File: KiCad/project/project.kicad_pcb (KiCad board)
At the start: 4 copper layers, 40 x 45 mm, 29 parts, among them P1 TB002-500-05BE, U1 DRV8313PWPR

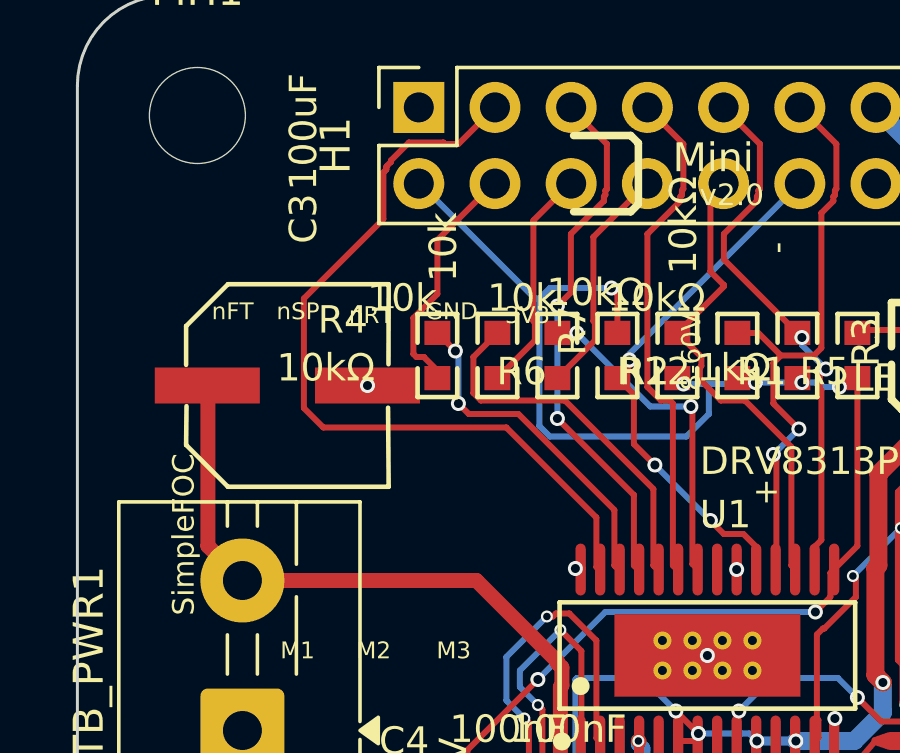
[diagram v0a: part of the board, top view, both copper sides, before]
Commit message: PCB: clear the last C3/R4 overlap (move R4 up, re-route EN1/EN1H)
The bulk cap C3's 9.4mm courtyard / 3.5mm-wide GND pad collided with the
leftmost EN resistor R4 (1 courtyard_overlap + 1 clearance 0.148mm). C3 is
boxed (IN1 routing below-left, board edge left), and the EN row is packed
at 2mm pitch against R12, so neither could shift toward the other.

Moved R4 up 1.6mm (146,100 -> 146,98.4) so its courtyard clears C3's
Y-band entirely, then re-routed its two simple 2-point nets EN1 (U1.26<->R4.2)
and EN1H (H1.4<->R4.1).

Result: 0 error-severity DRC items (was 2), 0 shorts, 0 unconnected, all 92
nets connected, net parity unchanged. The board is now electrically clean;
the 249 remaining DRC items are all cosmetic warnings (silk overlap/over
copper, text height, HTSSOP padstack) -- import artifacts to be cleaned in
a separate silk/text pass.

Co-Authored-By: Claude Opus 4.8 (1M context) <noreply@anthropic.com>
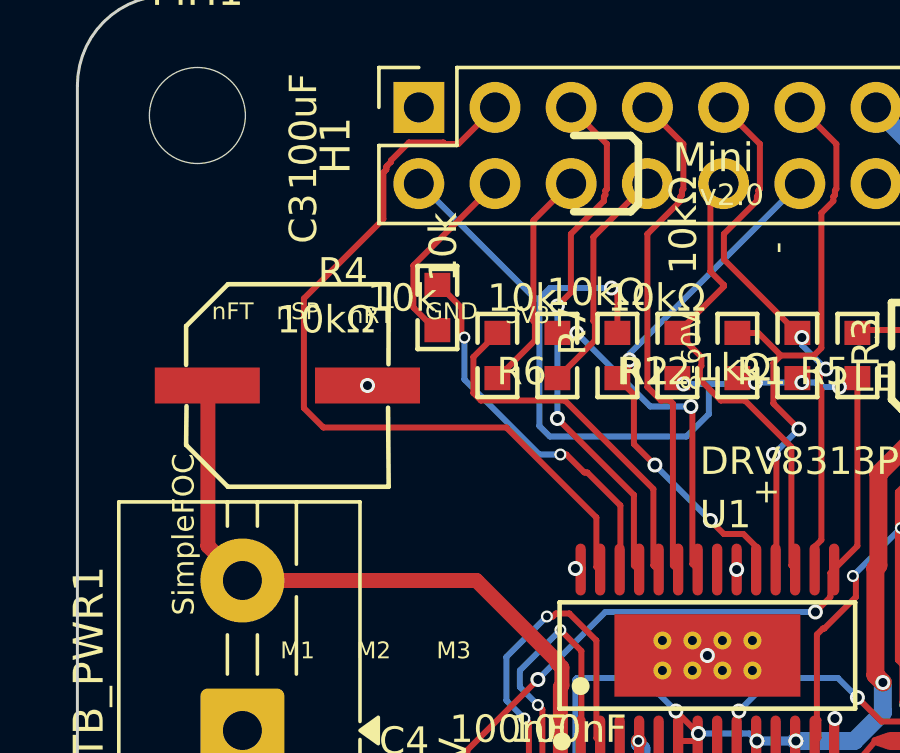
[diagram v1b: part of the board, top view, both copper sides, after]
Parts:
- moved R4 1.60 mm to (146.0, 98.4)
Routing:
- net EN1H: track 8.12 -> 6.43 mm
- net EN1: track 11.4 -> 12.7 mm
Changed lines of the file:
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@@
 	(footprint "R0603"
 		(layer "F.Cu")
-		(at 146 100 90)
+		(at 146 98.4 90)
 		(property "Reference" "R4"
 			(at 1.7221 -3.9853 0)
@@
 			(polygon
 				(pts
-					(xy 136.805 100.45) (xy 137.605 100.45) (xy 137.655 100.4) (xy 137.655 100.172) (xy 137.285 100.172)
-					(xy 137.285 99.842) (xy 137.655 99.842) (xy 137.655 99.6) (xy 137.605 99.55) (xy 136.805 99.55)
-					(xy 136.755 99.6) (xy 136.755 100.4)
+					(xy 136.805 98.85) (xy 137.605 98.85) (xy 137.655 98.8) (xy 137.655 98.572) (xy 137.285 98.572)
+					(xy 137.285 98.242) (xy 137.655 98.242) (xy 137.655 98) (xy 137.605 97.95) (xy 136.805 97.95) (xy 136.755 98)
+					(xy 136.755 98.8)
 				)
 			)
@@
 			(polygon
 				(pts
-					(xy 138.355 100.4) (xy 138.355 100.172) (xy 138.735 100.172) (xy 138.735 99.842) (xy 138.355 99.842)
-					(xy 138.355 99.6) (xy 138.405 99.55) (xy 139.195 99.55) (xy 139.245 99.6) (xy 139.245 100.4) (xy 139.195 100.45)
-					(xy 138.405 100.45)
+					(xy 138.355 98.8) (xy 138.355 98.572) (xy 138.735 98.572) (xy 138.735 98.242) (xy 138.355 98.242)
+					(xy 138.355 98) (xy 138.405 97.95) (xy 139.195 97.95) (xy 139.245 98) (xy 139.245 98.8) (xy 139.195 98.85)
+					(xy 138.405 98.85)
 				)
 			)
@@
 			(polygon
 				(pts
-					(xy 138.8 99.6) (xy 138.8 100.4) (xy 137.2 100.4) (xy 137.2 99.6)
+					(xy 138.8 98) (xy 138.8 98.8) (xy 137.2 98.8) (xy 137.2 98)
 				)
 			)
@@
 			(polygon
 				(pts
-					(xy 137.2 99.6) (xy 137.2 100.4) (xy 137.5 100.4) (xy 137.5 99.6)
+					(xy 137.2 98) (xy 137.2 98.8) (xy 137.5 98.8) (xy 137.5 98)
 				)
 			)
@@
 			(polygon
 				(pts
-					(xy 138.8 99.6) (xy 138.8 100.4) (xy 138.5 100.4) (xy 138.5 99.6)
+					(xy 138.8 98) (xy 138.8 98.8) (xy 138.5 98.8) (xy 138.5 98)
 				)
 			)
@@
 	)
 	(segment
-		(start 152.0749 107.1344)
-		(end 152.05 107.15)
+		(start 146 97.6)
+		(end 146 97.6466)
 		(width 0.2)
 		(layer "F.Cu")
@@
 	)
 	(segment
-		(start 152.05 107.15)
-		(end 151.9 107)
+		(start 146.8 98.4)
+		(end 146 97.6)
 		(width 0.2)
 		(layer "F.Cu")
@@
 	)
 	(segment
-		(start 151.9 105.15)
-		(end 148.7 101.95)
+		(start 146.9 99.4)
+		(end 146.8 99.3)
 		(width 0.2)
 		(layer "F.Cu")
@@
 	)
 	(segment
-		(start 151.9 107)
-		(end 151.9 105.15)
+		(start 146.8 99.3)
+		(end 146.8 98.4)
+		(width 0.2)
+		(layer "F.Cu")
+		(net "EN1")
+	)
+	(segment
+		(start 152.0749 107.1344)
+		(end 152.1 107.1)
 		(width 0.2)
 		(layer "F.Cu")
@@
 	)
 	(segment
-		(start 148.7 101.95)
-		(end 147.05 101.95)
+		(start 151 103.9)
+		(end 150.9 103.9)
 		(width 0.2)
 		(layer "F.Cu")
@@
 	)
 	(segment
-		(start 146.6 99.85)
-		(end 146 99.25)
+		(start 152.1 105)
+		(end 151 103.9)
 		(width 0.2)
 		(layer "F.Cu")
@@
 	)
 	(segment
-		(start 147.05 101.95)
-		(end 146.7 101.6)
+		(start 152.1 107.1)
+		(end 152.1 105)
+		(width 0.2)
+		(layer "F.Cu")
+		(net "EN1")
+	)
+	(segment
+		(start 150.9 103.9)
+		(end 150.3 103.3)
+		(width 0.2)
+		(layer "F.Cu")
+		(net "EN1")
+	)
+	(segment
+		(start 150.3 103.3)
+		(end 150.1 103.3)
 		(width 0.2)
 		(layer "F.Cu")
@@
 	)
 	(via
-		(at 146.7 101.6)
-		(size 0.5)
-		(drill 0.3)
+		(at 150.1 103.3)
+		(size 0.4)
+		(drill 0.25)
 		(layers "F.Cu" "B.Cu")
 		(tenting
@@
 	)
 	(via
-		(at 146.6 99.85)
-		(size 0.5)
-		(drill 0.3)
+		(at 146.9 99.4)
+		(size 0.4)
+		(drill 0.25)
 		(layers "F.Cu" "B.Cu")
 		(tenting
@@
 	)
 	(segment
-		(start 146.7 99.95)
-		(end 146.6 99.85)
+		(start 146.9 100.8)
+		(end 146.9 99.4)
 		(width 0.2)
 		(layer "B.Cu")
@@
 	)
 	(segment
-		(start 146.7 101.6)
-		(end 146.7 99.95)
+		(start 149.4 103.3)
+		(end 146.9 100.8)
+		(width 0.2)
+		(layer "B.Cu")
+		(net "EN1")
+	)
+	(segment
+		(start 150.1 103.3)
+		(end 149.4 103.3)
 		(width 0.2)
 		(layer "B.Cu")
@@
 	)
 	(segment
-		(start 146 97.95)
-		(end 145.2 98.75)
-		(width 0.2)
-		(layer "F.Cu")
-		(net "EN1H")
-	)
-	(segment
-		(start 145.2 98.75)
-		(end 145.2 99.95)
-		(width 0.2)
-		(layer "F.Cu")
-		(net "EN1H")
-	)
-	(segment
 		(start 147.92 94.27)
-		(end 147.9 94.25)
-		(width 0.2)
-		(layer "F.Cu")
-		(net "EN1H")
-	)
-	(segment
-		(start 146 96.15)
-		(end 146 97.95)
-		(width 0.2)
-		(layer "F.Cu")
-		(net "EN1H")
-	)
-	(segment
-		(start 147.9 94.25)
-		(end 146 96.15)
+		(end 147.9 94.3)
 		(width 0.2)
 		(layer "F.Cu")
@@
 	)
 	(segment
-		(start 145.55 100.05)
-		(end 146 100.5)
+		(start 147.9 94.3)
+		(end 145.2 97)
 		(width 0.2)
 		(layer "F.Cu")
@@
 	)
 	(segment
-		(start 145.2 99.95)
-		(end 145.3 100.05)
+		(start 145.2 98.4)
+		(end 146 99.2)
 		(width 0.2)
 		(layer "F.Cu")
@@
 	)
 	(segment
-		(start 145.3 100.05)
-		(end 145.55 100.05)
+		(start 146 99.2)
+		(end 146 99.1534)
 		(width 0.2)
 		(layer "F.Cu")
@@
 	)
 	(segment
-		(start 146 100.5)
-		(end 146 100.75)
+		(start 145.2 97)
+		(end 145.2 98.4)
 		(width 0.2)
 		(layer "F.Cu")

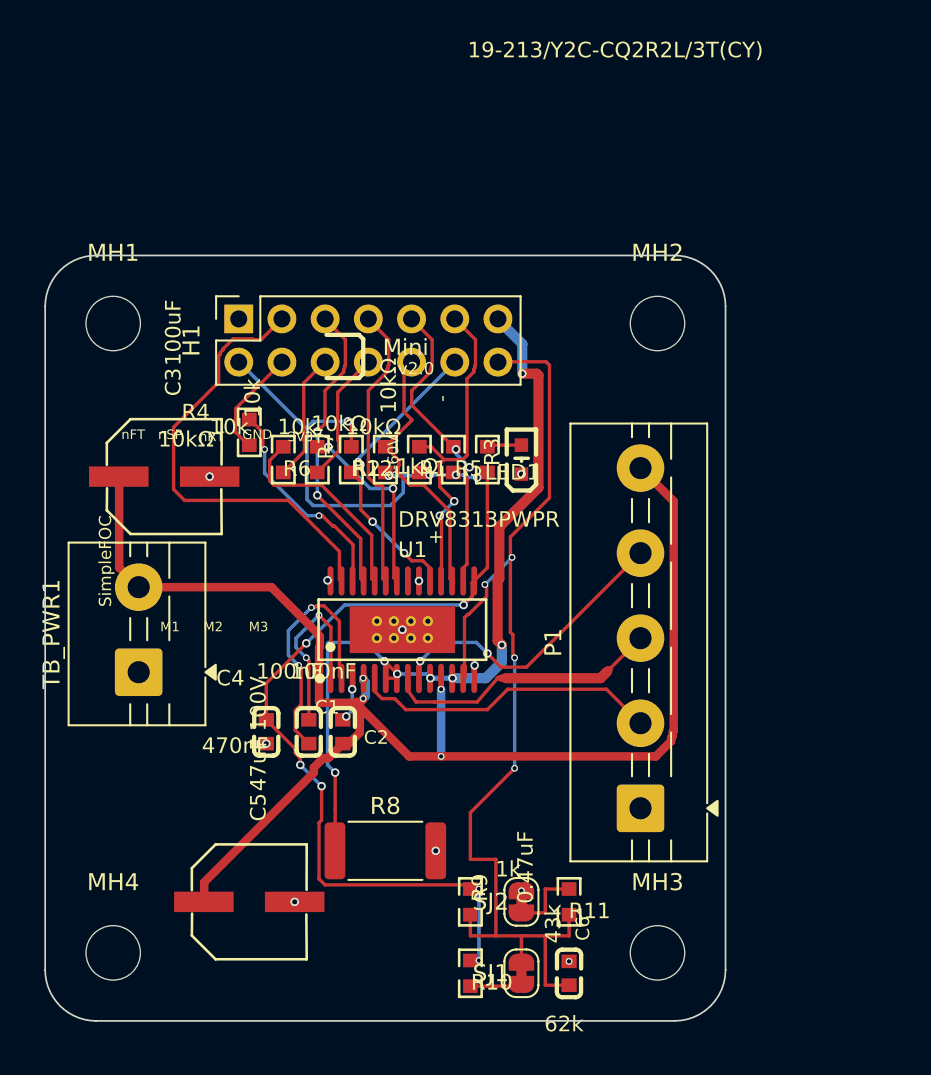
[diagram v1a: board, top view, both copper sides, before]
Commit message: Silk: full cleanup pass — 249 -> 6 cosmetic DRC warnings
Headless pcbnew. Electrical content untouched (97 pads, 0 net mismatches
vs prior; 0 unconnected). Silk/text only + one real assembly fix.

- Hid all redundant silk value fields (kept refs); hid the 4 mounting-hole
  refs (2 were clipping the edge).
- Deleted 37 stale connector pin-labels left over from the 26mm/2x5-header
  layout (they floated over the wrong parts post-relayout) and regenerated
  correct ones from the netlist: H1 2x7 (GND/3V3/IN1/EN1/IN2/EN2/IN3/EN3/
  RST/SLP/FLT/CMP/PGND/VREF), P1 motor (VM/M3/M2/M1/GND), TB_PWR1 (+/-).
- FIXED A REAL DEFECT: all 11 R0603 resistors had solder_paste_margin
  = -100mm (EasyEDA import garbage) -> no stencil aperture would be
  generated -> reflow couldn't paste them. Set to 0 (22 padstack warnings).
- Repositioned overlapping refs in the dense R-cluster / divider; deleted
  24 stray board-level silk shapes (H1-pin fragments + a redundant bottom
  logo over TB_PWR1's pad); relocated branding off parts.
- Removed C4 (non-polarized 0603) and H1 outlines that grazed their own
  pads; added '+' polarity marks for C3/C5 (polarized BD6.3).
- Relaxed min_text_height 0.8 -> 0.5mm to keep the small connector labels
  (matches the original board's 0.56mm silk; fab-producible).

Remaining 6 are pre-existing, footprint-intrinsic warnings (present on the
original import): 4 "silkscreen clipped by solder mask" pad entries that
report NO silk item and persist with all nearby silk removed, plus 2
item-less silk_overlap phantoms. Not addressable via silk editing.

Co-Authored-By: Claude Opus 4.8 (1M context) <noreply@anthropic.com>
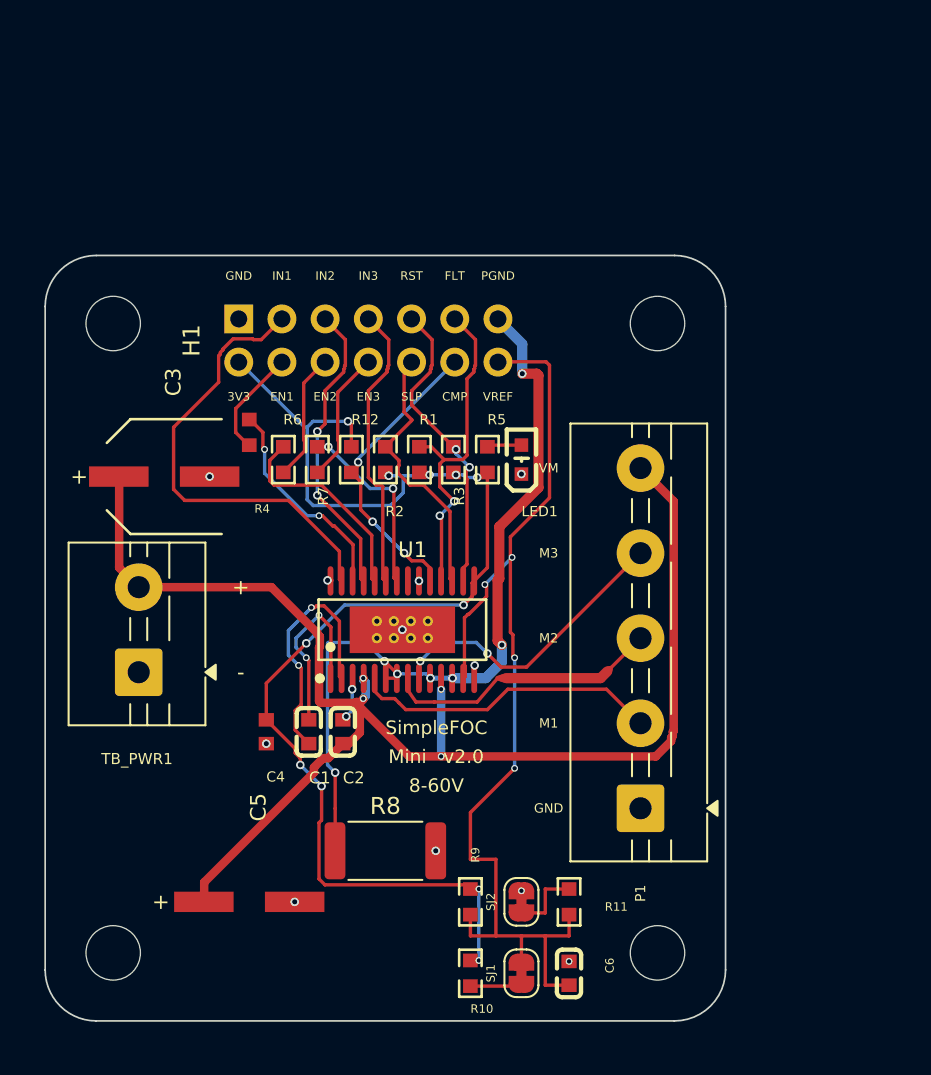
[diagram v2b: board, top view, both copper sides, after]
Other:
- board text added: "CMP"
- board text added: "EN1"
- board text added: "EN2"
- board text added: "EN3"
- board text added: "FLT"
- board text added: "PGND"
- board text added: "RST"
- board text added: "SLP"
- board text added: "VM"
- board text added: "VREF"
- board text removed: "EN"
- board text removed: "nFT"
- board text removed: "nRT"
- board text removed: "nSP"

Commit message: Footprints: back-annotate + library re-link (footprint_symbol_mismatch 29 -> 0)
Schematic Footprint fields were empty (footprints lived only in the PCB),
producing 29 footprint_symbol_mismatch parity items. Cleared all 29 headless
(pcbnew + kicad-skip); 0 unconnected, 0 error-severity DRC, 97 pads stable.

- 25x empty Footprint field, 2x stale PCB value text (C1 -> 10nF 100V,
  C3 -> 47uF 100V; PCB still read the v1.1 values), 2x SJ1/SJ2 BOM attr
  (excluded from BOM to match the SolderJumper footprint).
- Bare-name back-annotation alone just moves the problem to ERC (+25
  footprint_link_issues), since the embedded EasyEDA footprints have no
  library home. Fixed by giving them real lib:name homes on both sides:
  - 6 standard-origin footprints re-linked to canonical KiCad libs
    (Connector_PinSocket_2.54mm, TerminalBlock, Resistor_SMD, Jumper,
    MountingHole).
  - 5 EasyEDA footprints (C0603, R0603, LED0603-R-RD, CAP-SMD_BD6.3,
    HTSSOP-28) have no clean canonical match (geometry-verified) -> new
    project library KiCad/project/simplefocmini.pretty + project fp-lib-table.
- Result: footprint_symbol_mismatch 29 -> 0, ERC back to 141 baseline
  (footprint_link 25 -> 0). Re-linking surfaces 20 benign lib_footprint_mismatch
  FYIs (customized board footprints vs stock library) - left as-is.

Co-Authored-By: Claude Opus 4.8 (1M context) <noreply@anthropic.com>
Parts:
- C1: value 100nF -> 10nF 100V; footprint C0603 -> simplefocmini:C0603
- C2, C4, C6: footprint C0603 -> simplefocmini:C0603
- C3: value 100uF -> 47uF 100V; footprint CAP-SMD_BD6.3-L6.6-W6.6-FD -> simplefocmini:CAP-SMD_BD6.3-L6.6-W6.6-FD
- C5: footprint CAP-SMD_BD6.3-L6.6-W6.6-FD -> simplefocmini:CAP-SMD_BD6.3-L6.6-W6.6-FD
- H1: footprint PinSocket_2x07_P2.54mm_Vertical -> Connector_PinSocket_2.54mm:PinSocket_2x07_P2.54mm_Vertical
- LED1: footprint LED0603-R-RD -> simplefocmini:LED0603-R-RD
- MH1, MH2, MH3, MH4: footprint MountingHole_3.2mm_M3 -> MountingHole:MountingHole_3.2mm_M3
- P1: footprint TerminalBlock_MaiXu_MX126-5.0-05P_1x05_P5.00mm -> TerminalBlock:TerminalBlock_MaiXu_MX126-5.0-05P_1x05_P5.00mm
- R1, R10, R11, R12, R2, R3, R4, R5, R6, R7, R9: footprint R0603 -> simplefocmini:R0603
- R8: footprint R_2512_6332Metric -> Resistor_SMD:R_2512_6332Metric
- SJ1, SJ2: footprint SolderJumper-2_P1.3mm_Bridged_RoundedPad1.0x1.5mm -> Jumper:SolderJumper-2_P1.3mm_Bridged_RoundedPad1.0x1.5mm
- TB_PWR1: footprint TerminalBlock_MaiXu_MX126-5.0-02P_1x02_P5.00mm -> TerminalBlock:TerminalBlock_MaiXu_MX126-5.0-02P_1x02_P5.00mm
- U1: footprint HTSSOP-28_L9.8-W4.5-P0.65-LS6.6-BL-EP -> simplefocmini:HTSSOP-28_L9.8-W4.5-P0.65-LS6.6-BL-EP
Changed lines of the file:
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@@
 		)
 	)
-	(footprint "MountingHole_3.2mm_M3"
+	(footprint "MountingHole:MountingHole_3.2mm_M3"
 		(locked yes)
 		(layer "F.Cu")
@@
 		(embedded_fonts no)
 	)
-	(footprint "C0603"
+	(footprint "simplefocmini:C0603"
 		(layer "F.Cu")
 		(at 164.8 130.199999 90)
@@
 		)
 	)
-	(footprint "R0603"
+	(footprint "simplefocmini:R0603"
 		(layer "F.Cu")
 		(at 160 100 90)
@@
 		)
 	)
-	(footprint "C0603"
+	(footprint "simplefocmini:C0603"
 		(layer "F.Cu")
 		(at 151.5 116 90)
@@
 		)
 	)
-	(footprint "CAP-SMD_BD6.3-L6.6-W6.6-FD"
+	(footprint "simplefocmini:CAP-SMD_BD6.3-L6.6-W6.6-FD"
 		(layer "F.Cu")
 		(at 141 101)
@@
 			)
 		)
-		(property "Value" "100uF"
+		(property "Value" "47uF 100V"
 			(at 0 -6.5024 90)
 			(layer "F.SilkS")
@@
 		)
 	)
-	(footprint "R0603"
+	(footprint "simplefocmini:R0603"
 		(layer "F.Cu")
 		(at 152 100 90)
@@
 		)
 	)
-	(footprint "MountingHole_3.2mm_M3"
+	(footprint "MountingHole:MountingHole_3.2mm_M3"
 		(locked yes)
 		(layer "F.Cu")
@@
 		(embedded_fonts no)
 	)
-	(footprint "TerminalBlock_MaiXu_MX126-5.0-02P_1x02_P5.00mm"
+	(footprint "TerminalBlock:TerminalBlock_MaiXu_MX126-5.0-02P_1x02_P5.00mm"
 		(locked yes)
 		(layer "F.Cu")
@@
 		)
 	)
-	(footprint "R0603"
+	(footprint "simplefocmini:R0603"
 		(layer "F.Cu")
 		(at 159 126 -90)
@@
 		)
 	)
-	(footprint "SolderJumper-2_P1.3mm_Bridged_RoundedPad1.0x1.5mm"
+	(footprint "Jumper:SolderJumper-2_P1.3mm_Bridged_RoundedPad1.0x1.5mm"
 		(layer "F.Cu")
 		(at 162 130.199999 90)
@@
 		(embedded_fonts no)
 	)
-	(footprint "TerminalBlock_MaiXu_MX126-5.0-05P_1x05_P5.00mm"
+	(footprint "TerminalBlock:TerminalBlock_MaiXu_MX126-5.0-05P_1x05_P5.00mm"
 		(locked yes)
 		(layer "F.Cu")
@@
 		)
 	)
-	(footprint "HTSSOP-28_L9.8-W4.5-P0.65-LS6.6-BL-EP"
+	(footprint "simplefocmini:HTSSOP-28_L9.8-W4.5-P0.65-LS6.6-BL-EP"
 		(locked yes)
 		(layer "F.Cu")
@@
 		)
 	)
-	(footprint "C0603"
+	(footprint "simplefocmini:C0603"
 		(layer "F.Cu")
 		(at 147 116 90)
@@
 		)
 	)
-	(footprint "R0603"
+	(footprint "simplefocmini:R0603"
 		(layer "F.Cu")
 		(at 158 100 90)
@@
 		)
 	)
-	(footprint "MountingHole_3.2mm_M3"
+	(footprint "MountingHole:MountingHole_3.2mm_M3"
 		(locked yes)
 		(layer "F.Cu")
@@
 		(embedded_fonts no)
 	)
-	(footprint "R0603"
+	(footprint "simplefocmini:R0603"
 		(layer "F.Cu")
 		(at 150 100 90)
@@
 		)
 	)
-	(footprint "R_2512_6332Metric"
+	(footprint "Resistor_SMD:R_2512_6332Metric"
 		(layer "F.Cu")
 		(at 154 123)
@@
 		)
 	)
-	(footprint "R0603"
+	(footprint "simplefocmini:R0603"
 		(layer "F.Cu")
 		(at 148 100 90)
@@
 		)
 	)
-	(footprint "PinSocket_2x07_P2.54mm_Vertical"
+	(footprint "Connector_PinSocket_2.54mm:PinSocket_2x07_P2.54mm_Vertical"
 		(locked yes)
 		(layer "F.Cu")
@@
 		)
 	)
-	(footprint "R0603"
+	(footprint "simplefocmini:R0603"
 		(layer "F.Cu")
 		(at 154 100 90)
@@
 		)
 	)
-	(footprint "R0603"
+	(footprint "simplefocmini:R0603"
 		(layer "F.Cu")
 		(at 156 100 90)
@@
 		)
 	)
-	(footprint "R0603"
+	(footprint "simplefocmini:R0603"
 		(layer "F.Cu")
 		(at 159 130.199999 -90)
@@
 		)
 	)
-	(footprint "MountingHole_3.2mm_M3"
+	(footprint "MountingHole:MountingHole_3.2mm_M3"
 		(locked yes)
 		(layer "F.Cu")
@@
 		(embedded_fonts no)
 	)
-	(footprint "CAP-SMD_BD6.3-L6.6-W6.6-FD"
+	(footprint "simplefocmini:CAP-SMD_BD6.3-L6.6-W6.6-FD"
 		(layer "F.Cu")
 		(at 146 126)
@@
 		)
 	)
-	(footprint "R0603"
+	(footprint "simplefocmini:R0603"
 		(layer "F.Cu")
 		(at 164.8 126 90)
@@
 		)
 	)
-	(footprint "R0603"
+	(footprint "simplefocmini:R0603"
 		(layer "F.Cu")
 		(at 146 98.4 90)
@@
 		)
 	)
-	(footprint "SolderJumper-2_P1.3mm_Bridged_RoundedPad1.0x1.5mm"
+	(footprint "Jumper:SolderJumper-2_P1.3mm_Bridged_RoundedPad1.0x1.5mm"
 		(layer "F.Cu")
 		(at 162 126 90)
@@
 		(embedded_fonts no)
 	)
-	(footprint "LED0603-R-RD"
+	(footprint "simplefocmini:LED0603-R-RD"
 		(layer "F.Cu")
 		(at 162 100 90)
@@
 		)
 	)
-	(footprint "C0603"
+	(footprint "simplefocmini:C0603"
 		(layer "F.Cu")
 		(at 149.5 116 90)
@@
 			)
 		)
-		(property "Value" "100nF"
+		(property "Value" "10nF 100V"
 			(at 4.0792 -3.0963 180)
 			(layer "F.SilkS")
